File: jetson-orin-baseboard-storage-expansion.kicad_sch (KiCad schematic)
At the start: 0 parts

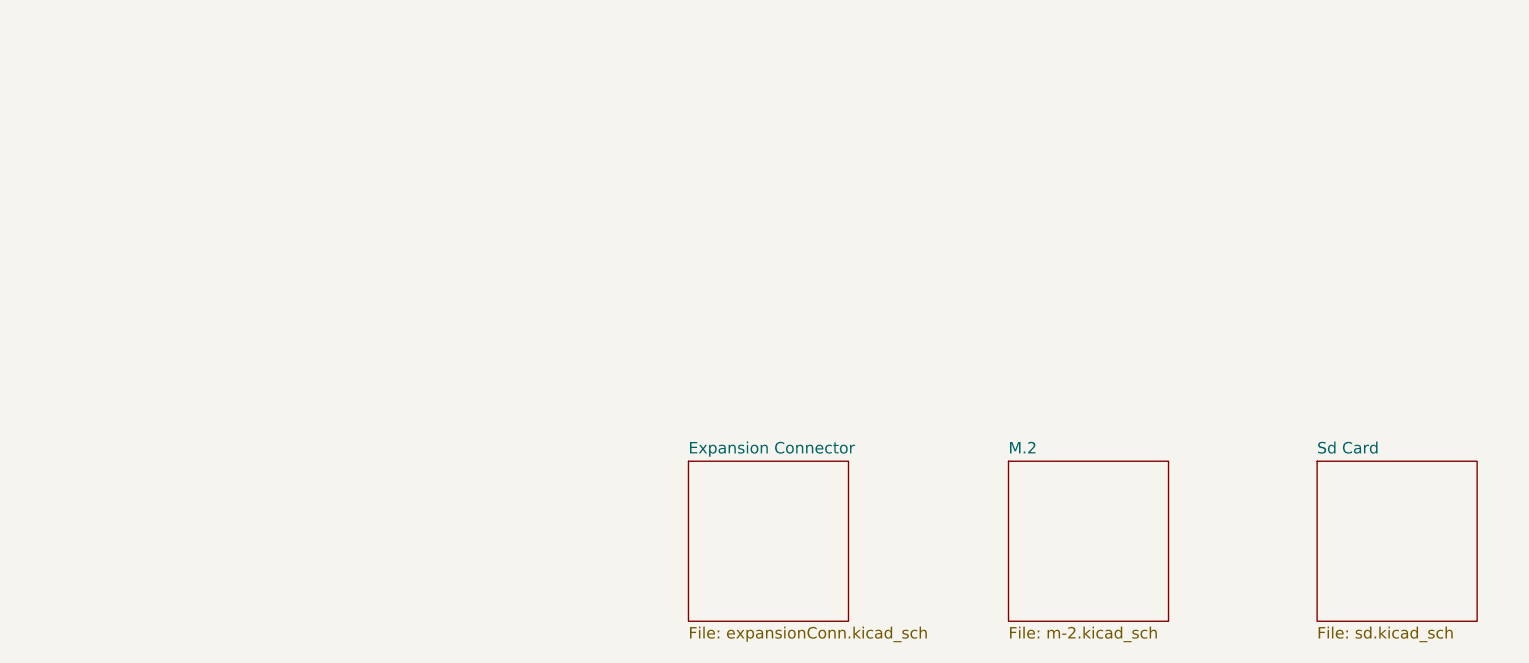
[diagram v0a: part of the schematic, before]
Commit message: Add layout for expansion connector and M.2 key M slot
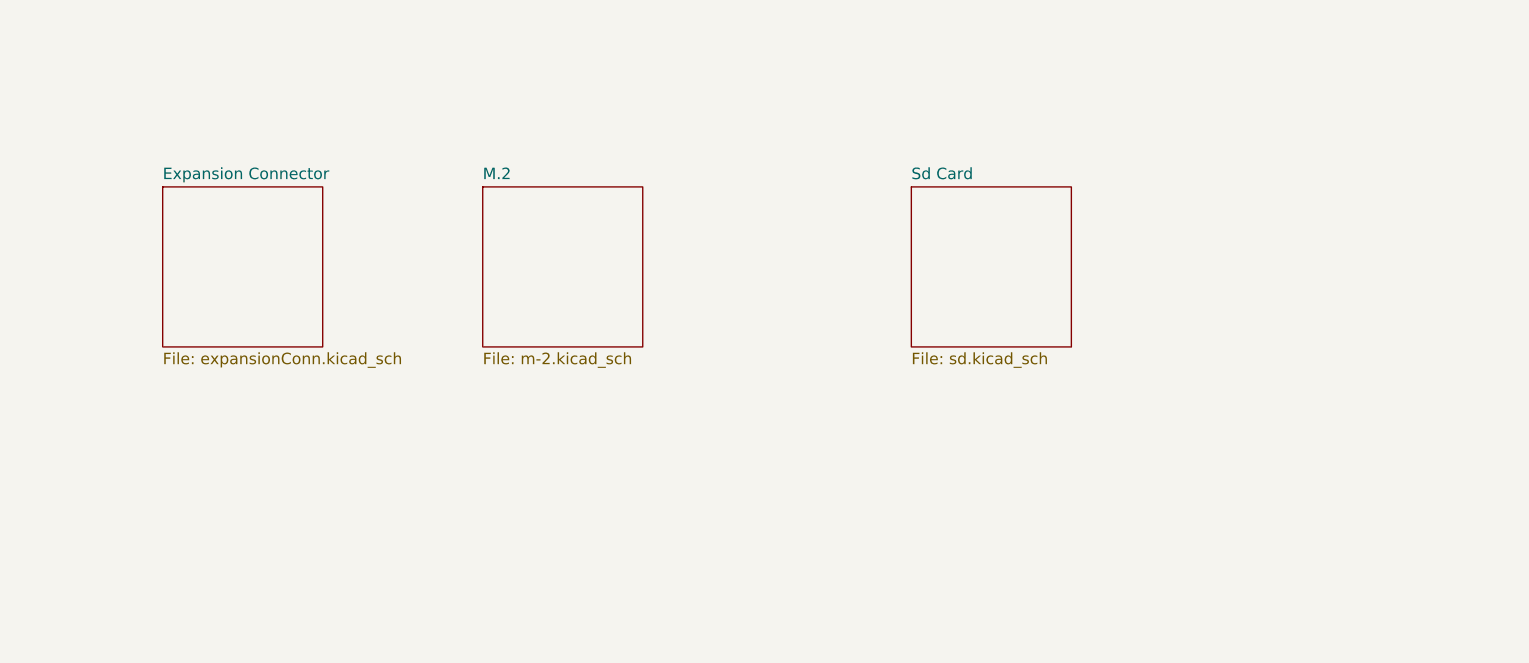
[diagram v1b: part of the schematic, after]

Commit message: [#45539] Apply changes after review
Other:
- sheet Sd Card renamed SD Card
- sheet Expansion Connector: file expansionConn.kicad_sch -> expansion-conn.kicad_sch
